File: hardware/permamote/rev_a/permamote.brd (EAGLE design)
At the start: 27 x 60.1 mm, 99 parts, among them J1 TC2030-JLINK-NL, J2 M10X2, J3 M04X2, J5 MICRO_USB_B_HIROSE_ZX62R-B-5P, Q1 PMDXB950UPEL, Q10 PMDXB950UPEL, Q2 PMDXB950UPEL, Q3 PMDXB950UPEL, Q4 PMDXB950UPEL, Q5 PMDXB950UPEL, Q6 PMDXB950UPEL, Q7 PMDXB950UPEL, Q8 PMDXB950UPEL, U1 AB1815-T3, U10 NRF52840, U11 SI7021-A20-GM1, U12 FT232RQ, U2 BQ25505, U3 EKMB1101111, U4 ISL29125, U5 LIS2DW12, U6 MAX17222, U7 MAX44009, U8 MS5637-02BA03, X1 32MHz, X3 32.768kHz, X4 ABS07-32.768KHZ-7-T

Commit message: WIP reroute signals
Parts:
- C17: device passives:0603_CAP -> passives:0402_CAP
- C8: device passives:0402_CAP -> passives:0603_CAP
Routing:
- net GND: vias 40 -> 41
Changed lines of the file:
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@@
 <attribute name="VALUE" x="8.544" y="12.973" size="1.016" layer="27" font="vector" ratio="12" rot="R180" align="bottom-center"/>
 </element>
-<element name="C17" library="passives" package="0603_CAP" value="10nF" x="24.892" y="55.34" smashed="yes">
+<element name="C17" library="passives" package="0402_CAP" value="10nF" x="24.892" y="55.34" smashed="yes">
 <attribute name="DIGIKEY" value="490-4516-1-ND" x="24.892" y="55.34" size="1.778" layer="27" display="off"/>
 <attribute name="NAME" x="23.622" y="56.356" size="1.016" layer="25" font="vector" ratio="12" rot="R90" align="bottom-center"/>
@@
 <element name="C41" library="passives" package="0402_CAP" value="0.1uF" x="7.629" y="52.179" smashed="yes">
 <attribute name="DIGIKEY" value="490-6328-1-ND" x="8.629" y="52.179" size="1.778" layer="27" display="off"/>
-<attribute name="NAME" x="7.629" y="52.56" size="1.016" layer="25" font="vector" ratio="12" align="bottom-center"/>
+<attribute name="NAME" x="8.146" y="53.857" size="1.016" layer="25" font="vector" ratio="12" rot="R90" align="bottom-center"/>
 </element>
 <element name="Q7" library="fets" package="XDFN-6" value="PMDXB950UPEL" x="-7.318" y="20.88" smashed="yes" rot="R90">
@@
 <attribute name="NAME" x="18.034" y="50.133" size="1.016" layer="25" font="vector" ratio="12" align="bottom-center"/>
 </element>
-<element name="C8" library="passives" package="0402_CAP" value="4.7uF" x="25.146" y="53.054" smashed="yes">
+<element name="C8" library="passives" package="0603_CAP" value="4.7uF" x="25.146" y="53.054" smashed="yes">
 <attribute name="DIGIKEY" value="445-5947-1-ND" x="25.146" y="53.054" size="1.778" layer="27" display="off"/>
 <attribute name="NAME" x="25.146" y="53.435" size="1.016" layer="25" font="vector" ratio="12" align="bottom-center"/>
@@
 <wire x1="72.39" y1="47.117" x2="74.93" y2="47.117" width="0" layer="19" extent="1-1"/>
 <wire x1="70.993" y1="50.438" x2="72.39" y2="47.117" width="0" layer="19" extent="1-1"/>
-<wire x1="25.57906875" y1="53.054" x2="70.993" y2="50.438" width="0" layer="19" extent="1-1"/>
+<wire x1="25.796" y1="53.054" x2="70.993" y2="50.438" width="0" layer="19" extent="1-1"/>
 <wire x1="20.56306875" y1="8.671" x2="21.273" y2="8.29" width="0" layer="19" extent="1-1"/>
 <wire x1="20.328" y1="10.8248" x2="20.37" y2="10.104" width="0" layer="19" extent="1-1"/>
@@
 <wire x1="18.87" y1="12.854" x2="20.328" y2="10.8248" width="0" layer="19" extent="1-1"/>
 <wire x1="12.446" y1="19.558" x2="15.67306875" y2="21.082" width="0" layer="19" extent="1-1"/>
+<via x="22.098" y="50.26" extent="1-16" drill="0.2032"/>
 </signal>
 <signal name="N$8">
@@
 <contactref element="C17" pad="1"/>
 <contactref element="U2" pad="4"/>
-<wire x1="21.806" y1="53.554" x2="23.106" y2="53.554" width="0.4064" layer="1"/>
-<wire x1="24.242" y1="54.69" x2="24.242" y2="55.34" width="0.4064" layer="1"/>
-<wire x1="23.106" y1="53.554" x2="24.242" y2="54.69" width="0.4064" layer="1"/>
+<wire x1="21.806" y1="53.554" x2="22.606" y2="53.554" width="0.4064" layer="1"/>
+<wire x1="22.606" y1="53.554" x2="24.392" y2="55.34" width="0.4064" layer="1"/>
+<wire x1="24.392" y1="55.34" x2="24.45893125" y2="55.34" width="0.4064" layer="1"/>
 </signal>
 <signal name="N$31">

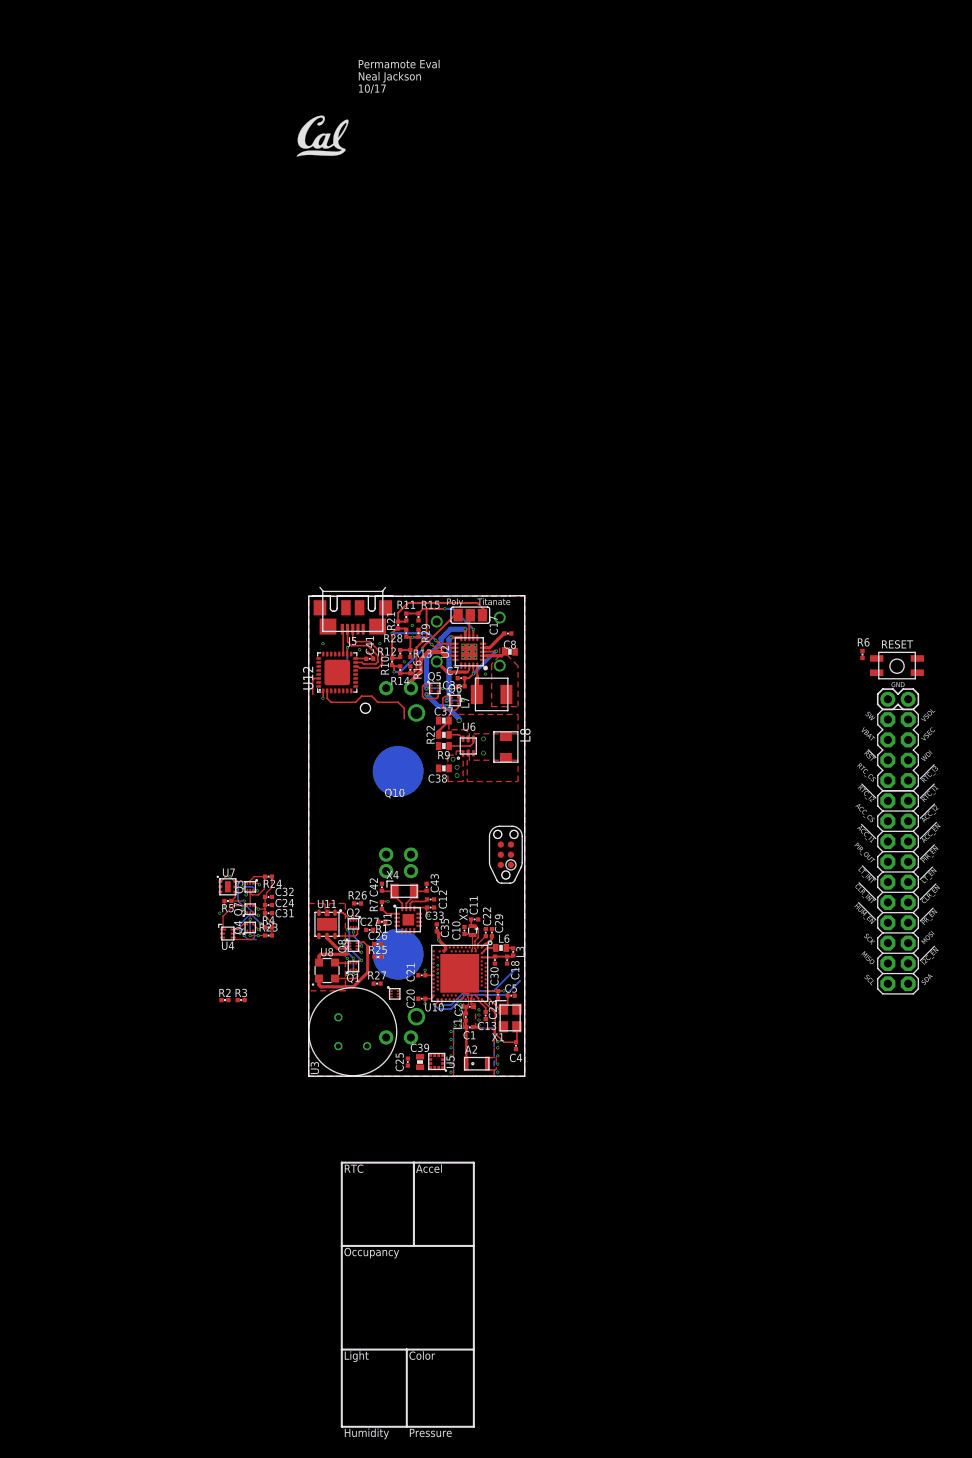
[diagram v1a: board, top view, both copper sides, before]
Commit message: No airwires
Add testpoints, connect dbg uart tx/rx lines
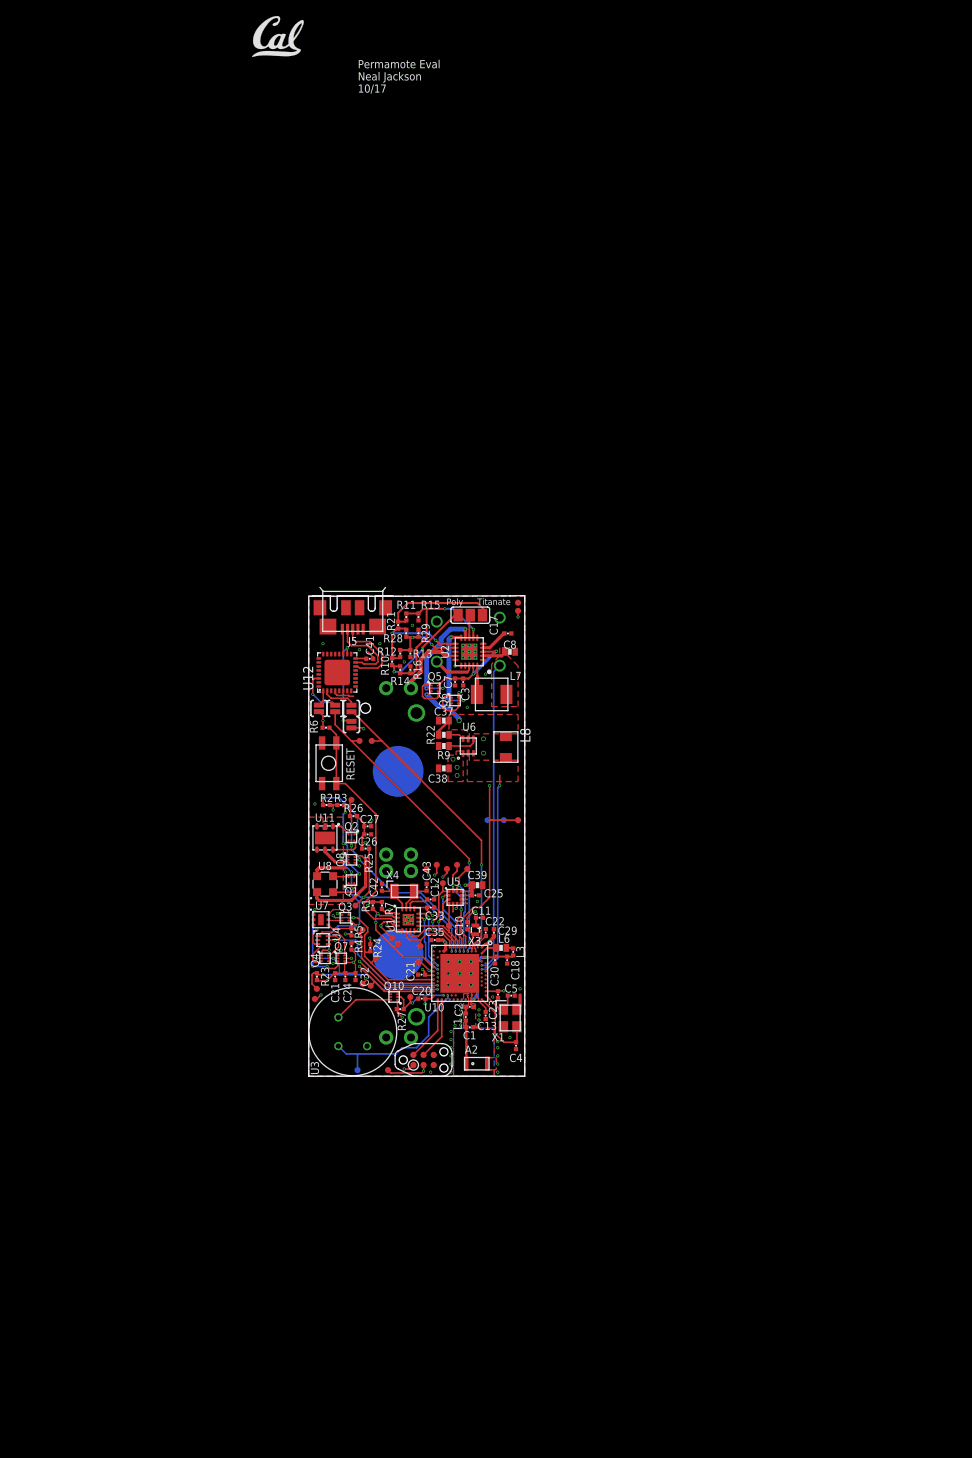
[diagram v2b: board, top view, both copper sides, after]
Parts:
- removed J2: M10X2, SparkFun-Connectors:2X10
- removed J3: M04X2, SparkFun-Connectors:2X4
- removed J4: (no value), SparkFun-Connectors:1X02
- added SJ2, SJ3, SJ4, SJ5: SOLDERJUMPERNC2, SparkFun-Passives:SJ_2S-NOTRACE
- added TP1, TP10, TP11, TP12, TP13, TP14, TP15, TP16, TP17, TP18, TP19, TP2, TP20, TP21, TP22, TP23, TP24, TP25, TP26, TP27, TP28, TP29, TP3, TP4, TP5, TP6, TP7, TP8, TP9: TEST-POINT3, headers:PAD.03X.03
- moved S1 72.0 mm to (2.54, 39.1), turned to 270 degrees
- moved R6 67.7 mm to (2.16, 43.6), turned to 180 degrees
- moved J1 27.6 mm to (14.4, 2.03), turned to 0 degrees
- moved R2 27.5 mm to (2.22, 33.9)
- moved R3 27.4 mm to (4.00, 33.9)
- moved C39 23.2 mm to (21.1, 23.9), turned to 0 degrees
- moved C25 22.5 mm to (20.8, 22.6), turned to 0 degrees
- moved U5 20.6 mm to (18.3, 22.4), turned to 0 degrees
- moved R5 15.9 mm to (5.33, 18.0), turned to 270 degrees
- moved R24 15.5 mm to (7.70, 16.1), turned to 90 degrees
- moved C32 14.7 mm to (5.84, 12.4), turned to 270 degrees
- moved C26 13.8 mm to (7.37, 30.2)
- moved U$1 13.6 mm to (-7.08, 127.4)
- moved R25 13.6 mm to (7.11, 28.4), turned to 180 degrees
- moved C24 13.1 mm to (4.57, 12.4), turned to 270 degrees
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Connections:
- removed net !ACC_EN: J2.15
- removed net !I2C_EN: J2.3
- new net !FTDI_RESET: SJ3.2, U12.18
- new net FTDI_VCCIO: SJ2.2, U12.1
- new net RXD: SJ4.1, U12.2
- new net TXD: SJ5.1, U12.30
- net !CLR_EN: now also TP11.P$1, U10.AC21; no longer J2.9, U10.T2
- net !CLR_INT: now also TP22.P$1, U10.AC19; no longer J2.10, U10.W24
- net !HUM_EN: now also TP14.P$1, U10.P2; no longer J2.8, U10.U1
- net !LT_EN: now also TP12.P$1, U10.AD16; no longer J2.11, U10.A16
- net !LT_INT: now also TP23.P$1, U10.AD18; no longer J2.12, U10.U24
- net !PIR_EN: now also TP13.P$1, U10.Y23; no longer J2.13, U10.A20
- net !PR_EN: now also TP10.P$1, U10.T2; no longer J2.7, U10.B19
- net !RST: now also SJ3.1, TP19.P$1; no longer J3.4, U10.AD12, U12.18
- net !RTC_IRQ1: now also TP15.P$1, U10.AC11; no longer J2.19, U10.AC9
- net !RTC_IRQ2: now also TP16.P$1, U10.AC15; no longer J2.20, U10.AD16
- net !RTC_IRQ3: now also TP17.P$1, U10.AD12; no longer J3.1, U10.P23
- net ACC_CS: now also TP9.P$1, U10.M2; no longer J2.18, U10.AD8
- net ACC_INT1: now also TP20.P$1, U10.L1; no longer J2.16, U10.R24
- net ACC_INT2: now also TP21.P$1, U10.K2; no longer J2.17, U10.L24
- net DBG_RX: now also SJ5.2, TP2.P$1, U10.G1; no longer U12.30
- net DBG_TX: now also SJ4.2, TP1.P$1, U10.H2; no longer U12.2
- net GND: now also TP29.P$1; no longer J4.1, J4.2
- net MISO: now also TP6.P$1, U10.U1; no longer J2.4, U10.AD22
- net MOSI: now also TP7.P$1, U10.N1; no longer J2.5, U10.AD20
- net PIR_OUT: now also TP24.P$1, U10.V23; no longer J2.14, U10.Y23
- net RTC_CS: now also TP8.P$1, U10.AC9; no longer J3.2, U10.AD10
- net SCK: now also TP5.P$1, U10.R1; no longer J2.6, U10.AD18
- net SCL: now also TP4.P$1, U10.AD20; no longer J2.2, U10.N1
- net SDA: now also TP3.P$1, U10.AD22; no longer J2.1, U10.L1
- net SW: now also TP27.P$1, U10.B11; no longer J3.8, U10.G1
- net VBAT: no longer J3.6, U10.J1
- net VCC: now also SJ2.1, TP28.P$1; no longer U12.1
- net VSEC: now also TP26.P$1, U10.J1; no longer J3.5, U10.A12
- net VSOL: now also TP25.P$1, U10.B9; no longer J3.7, U10.A10
- net WDI: now also TP18.P$1, U10.AD10; no longer J3.3, U10.A8
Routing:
- net !RST: track 6.73 -> 60.1 mm, vias 2 -> 4
- net SCL: track 4.10 -> 50.8 mm, vias 3 -> 7
- net VSEC: track 5.26 -> 49.4 mm, vias 0 -> 1
- net VSOL: track 2.33 -> 41.9 mm, vias 0 -> 1
- net DBG_RX: track 2.60 -> 37.4 mm, vias 0 -> 2
- net SDA: track 7.51 -> 41.0 mm, vias 4 -> 6
- net !RTC_EXTR: track 0.00 -> 31.2 mm
- net SW: track 0.00 -> 26.3 mm, vias 0 -> 2
- net DBG_TX: track 13.0 -> 38.9 mm, vias 0 -> 2
- net !PR_EN: track 6.47 -> 31.8 mm, vias 4 -> 5
- net !HUM_EN: track 3.97 -> 29.0 mm, vias 2 -> 4
- net !CLR_INT: track 6.21 -> 31.0 mm, vias 2 -> 4
- net GND: track 8.03 -> 30.4 mm, vias 41 -> 67
- net VCC: track 28.3 -> 49.7 mm, vias 16 -> 24
- net PIR_OUT: track 0.00 -> 20.7 mm, vias 0 -> 1
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- added copper zone on layer 15, net VBAT
- removed copper zone on layer 2, net VBAT
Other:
- board text removed: "!ACC_EN"
- board text removed: "!ACC_I1"
- board text removed: "!ACC_I2"
- board text removed: "!CLR_EN"
- board text removed: "!CLR_INT"
- board text removed: "!HUM_EN"
- board text removed: "!I2C_EN"
- board text removed: "!LT_EN"
- board text removed: "!LT_INT"
- board text removed: "!PIR_EN"
- board text removed: "!PR_EN"
- board text removed: "!RST"
- board text removed: "!RTC_I1"
- board text removed: "!RTC_I2"
- board text removed: "!RTC_I3"
- board text removed: "ACC_CS"
- board text removed: "Accel"
- board text removed: "Color"
- board text removed: "GND"
- board text removed: "Humidity"
- board text removed: "Light"
- board text removed: "MISO"
- board text removed: "MOSI"
- board text removed: "Occupancy"
- board text removed: "PIR_OUT"
- board text removed: "Pressure"
- board text removed: "RTC"
- board text removed: "RTC_CS"
- board text removed: "SCK"
- board text removed: "SCL"
- board text removed: "SDA"
- board text removed: "SW"
- board text removed: "VBAT"
- board text removed: "VSEC"
- board text removed: "VSOL"
- board text removed: "WDI"

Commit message: silk edits
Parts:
- added U$2: (no value), logos:UCB_CAL_200MIL
- U$1: device logos:UCB_CAL_200MIL -> logos:UCB_CAL_100MIL
- moved U$1 89.3 mm to (-9.91, 38.1)
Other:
- board text added: "Permamote Neal Jackson 1/18"
- board text removed: "Permamote Eval Neal Jackson 10/17"
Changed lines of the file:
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@@
 <wire x1="0" y1="60" x2="0" y2="0" width="0.1524" layer="23"/>
 <text x="4.699" y="38.989" size="1.016" layer="25" font="vector" ratio="12" rot="R270" align="bottom-center">RESET</text>
-<text x="6.128" y="127.011" size="1.016" layer="25" font="vector" ratio="12" align="top-left">Permamote Eval
+<text x="16.034" y="33.539" size="1.016" layer="25" font="vector" ratio="12" align="top-left">Permamote
 Neal Jackson
-10/17</text>
+1/18</text>
 <text x="21.082" y="58.896" size="0.8128" layer="25" font="vector" ratio="12">Titanate</text>
 <text x="19.304" y="58.896" size="0.8128" layer="25" font="vector" ratio="12" align="bottom-right">Poly</text>
@@
 <attribute name="MANUFACTURER" value="MPD" x="13.462" y="26.416" size="1.778" layer="28" rot="MR90" display="off"/>
 <attribute name="MPN" value="BH123A" x="13.462" y="26.416" size="1.778" layer="28" rot="MR90" display="off"/>
-<attribute name="NAME" x="23.462" y="3.416" size="1.016" layer="22" font="vector" ratio="12" rot="MR90"/>
+<attribute name="NAME" x="22.954" y="4.94" size="1.016" layer="22" font="vector" ratio="12" rot="MR90"/>
 </element>
 <element name="U4" library="chips" package="ODFN-6-1.5MMX1.6MM" value="ISL29125" x="1.778" y="17.018" smashed="yes">
@@
 <attribute name="VALUE" x="10.541" y="21.336" size="1.016" layer="27" font="vector" ratio="12" rot="R90" align="bottom-center"/>
 </element>
-<element name="U$1" library="logos" package="UCB_CAL_200MIL" value="" x="-7.08" y="127.392" smashed="yes"/>
 <element name="U3" library="chips" package="AMN2" value="EKMB1101111" x="5.496" y="5.558" smashed="yes">
 <attribute name="DIGIKEY" value="255-3065-ND" x="5.496" y="5.558" size="1.778" layer="27" display="off"/>
@@
 <attribute name="MANUFACTURER" value="Vishay Dale" x="24.638" y="41.148" size="1.778" layer="27" font="vector" ratio="12" rot="R270" display="off"/>
 <attribute name="MPN" value="IHLP1212BZER1R0M11" x="24.638" y="41.148" size="1.778" layer="27" font="vector" ratio="12" rot="R270" display="off"/>
-<attribute name="NAME" x="26.438" y="43.548" size="1.27" layer="25" rot="R270"/>
+<attribute name="NAME" x="23" y="43.456" size="1.016" layer="25" font="vector" ratio="12"/>
 </element>
 <element name="U12" library="ftdichip" library_urn="urn:adsk.eagle:library:231" package="QFN32" package3d_urn="urn:adsk.eagle:package:14014/1" value="FT232RQ" x="3.557" y="50.467" smashed="yes" rot="R90">
 <attribute name="MF" value="" x="3.557" y="50.467" size="1.778" layer="27" rot="R90" display="off"/>
 <attribute name="MPN" value="FT232RQ" x="3.557" y="50.467" size="1.778" layer="27" rot="R90" display="off"/>
-<attribute name="NAME" x="0.561" y="48.191" size="1.27" layer="25" rot="R90"/>
+<attribute name="NAME" x="1.27" y="53.34" size="1.016" layer="25" font="vector" ratio="12"/>
 <attribute name="OC_FARNELL" value="1146033" x="3.557" y="50.467" size="1.778" layer="27" rot="R90" display="off"/>
 <attribute name="OC_NEWARK" value="91K9919" x="3.557" y="50.467" size="1.778" layer="27" rot="R90" display="off"/>
@@
 <element name="TP28" library="headers" package="PAD.03X.03" value="TEST-POINT3" x="26.162" y="58.166"/>
 <element name="TP29" library="headers" package="PAD.03X.03" value="TEST-POINT3" x="26.162" y="59.182"/>
+<element name="U$1" library="logos" package="UCB_CAL_100MIL" value="" x="-9.906" y="38.1"/>
+<element name="U$2" library="logos" package="UCB_CAL_200MIL" value="" x="9.144" y="28.956"/>
 </elements>
 <signals>

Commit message: rearrange board
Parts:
- removed TP10, TP11, TP12, TP13, TP14, TP15, TP16, TP17, TP18, TP19, TP2, TP20, TP21, TP22, TP23, TP24, TP25, TP26, TP27, TP28, TP29, TP3, TP4, TP5, TP6, TP7, TP8, TP9: TEST-POINT3, headers:PAD.03X.03
- moved U$2 45.8 mm to (-26.2, 58.2)
- moved A2 30.2 mm to (25.5, 31.4), turned to 90 degrees
- moved U$1 29.9 mm to (-36.6, 51.6)
- moved U4 27.8 mm to (25.1, 2.03), turned to 90 degrees
- moved Q4 25.3 mm to (25.4, 5.08), turned to 90 degrees
- moved U7 25.2 mm to (19.8, 2.29), turned to 90 degrees
- moved J1 24.7 mm to (24.6, 24.5), turned to 90 degrees
- moved C39 24.3 mm to (13.0, 1.02), turned to 180 degrees
- moved R23 23.6 mm to (23.9, 6.60), turned to 180 degrees
- moved C4 23.2 mm to (12.7, 22.9)
- moved C25 22.4 mm to (15.7, 0.76)
- moved Q7 22.3 mm to (22.4, 2.03)
- moved Q3 21.0 mm to (19.6, 5.08), turned to 270 degrees
- moved C31 20.4 mm to (22.2, 4.70), turned to 90 degrees
- moved R4 20.4 mm to (23.9, 7.75), turned to 180 degrees
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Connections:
- net !CLR_EN: no longer TP11.P$1
- net !CLR_INT: no longer TP22.P$1
- net !HUM_EN: no longer TP14.P$1
- net !LT_EN: no longer TP12.P$1
- net !LT_INT: no longer TP23.P$1
- net !PIR_EN: no longer TP13.P$1
- net !PR_EN: no longer TP10.P$1
- net !RST: no longer TP19.P$1
- net !RTC_IRQ1: no longer TP15.P$1
- net !RTC_IRQ2: no longer TP16.P$1
- net !RTC_IRQ3: no longer TP17.P$1
- net ACC_CS: no longer TP9.P$1
- net ACC_INT1: no longer TP20.P$1
- net ACC_INT2: no longer TP21.P$1
- net DBG_RX: no longer TP2.P$1
- net GND: no longer TP29.P$1
- net MISO: no longer TP6.P$1
- net MOSI: no longer TP7.P$1
- net PIR_OUT: no longer TP24.P$1
- net RTC_CS: no longer TP8.P$1
- net SCK: no longer TP5.P$1
- net SCL: no longer TP4.P$1
- net SDA: no longer TP3.P$1
- net SW: no longer TP27.P$1
- net VCC: no longer TP28.P$1
- net VSEC: no longer TP26.P$1
- net VSOL: no longer TP25.P$1
- net WDI: no longer TP18.P$1
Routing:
- net !RST: track 60.1 -> 0.00 mm, vias 4 -> 1
- net VSOL: track 41.9 -> 3.40 mm
- net DBG_RX: track 37.4 -> 4.49 mm, vias 2 -> 0
- net DBG_TX: track 38.9 -> 6.79 mm, vias 2 -> 1
- net SW: track 26.3 -> 0.00 mm, vias 2 -> 1
- net VSEC: track 49.4 -> 23.5 mm
- net !PR_EN: track 31.8 -> 6.47 mm, vias 5 -> 4
- net !RTC_EXTR: track 31.2 -> 7.42 mm
- net !CLR_INT: track 31.0 -> 7.46 mm, vias 4 -> 3
- net SCL: track 50.8 -> 27.7 mm, vias 7 -> 5
- net !HUM_EN: track 29.0 -> 10.2 mm
- net !LT_EN: track 27.9 -> 12.0 mm
- net WDI: track 15.6 -> 0.21 mm, vias 2 -> 0
- net !RTC_IRQ2: track 15.1 -> 0.00 mm, vias 2 -> 1
- net RTC_CS: track 14.9 -> 0.00 mm, vias 3 -> 1
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- added copper zone on layer 1, net N$11
